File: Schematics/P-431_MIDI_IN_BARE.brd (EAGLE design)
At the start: 47.6 x 85.4 mm, 19 parts, among them X1 MIDI IN, X4 CTRL OUT and POWER

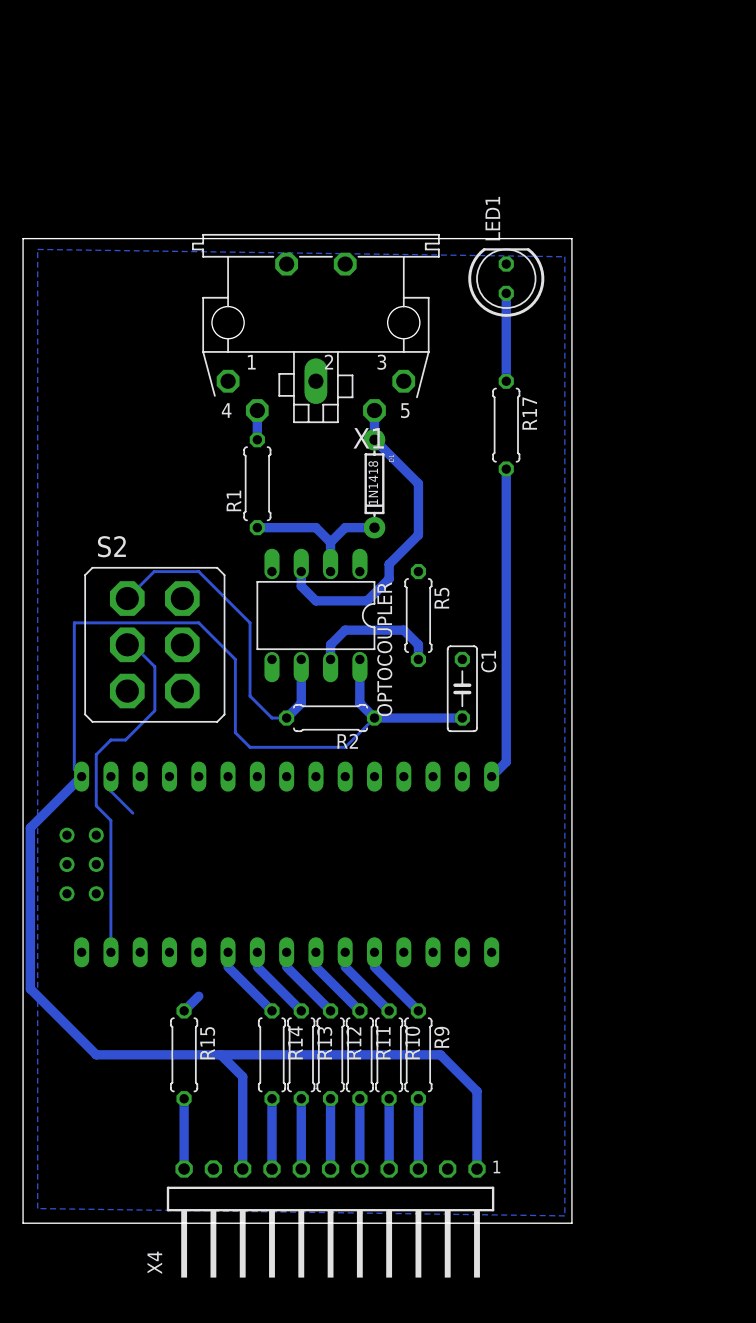
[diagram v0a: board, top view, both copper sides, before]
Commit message: Added reset pullup resistor and fixed resistors value for optocoupler
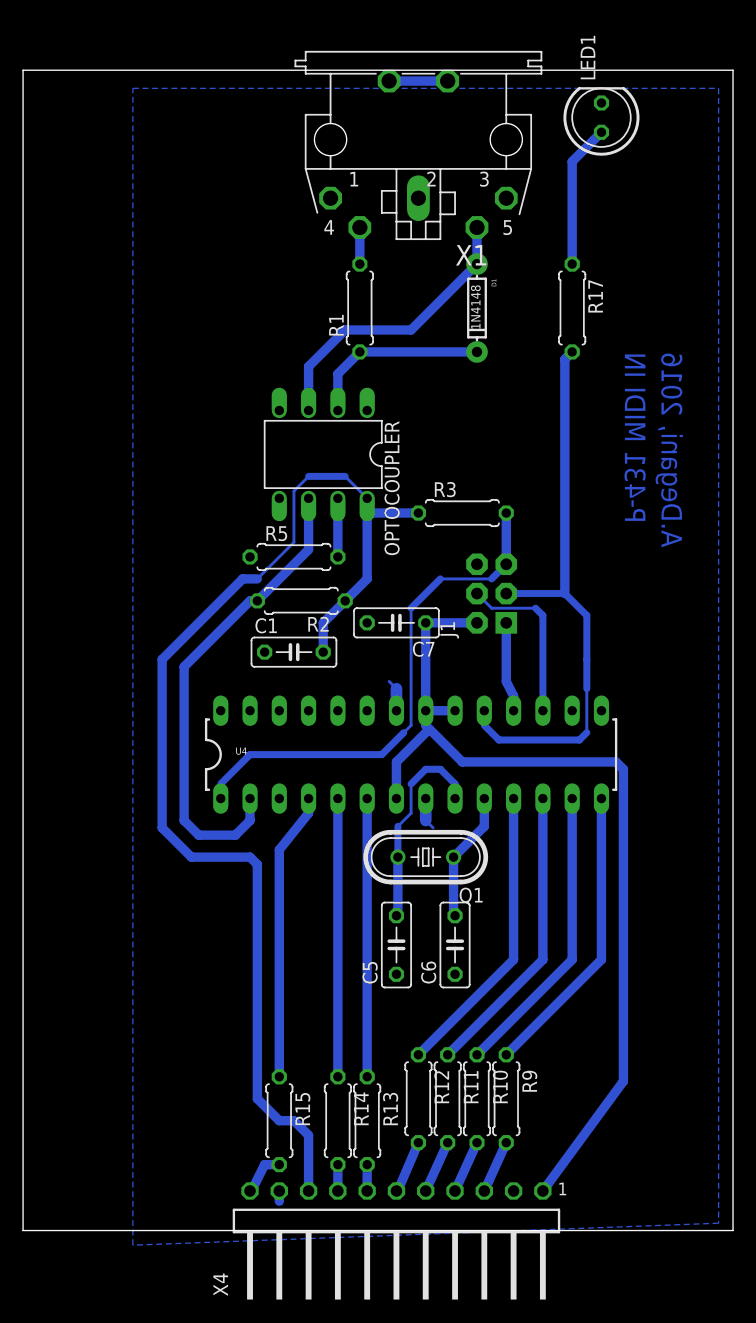
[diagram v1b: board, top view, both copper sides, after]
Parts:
- removed S2: PROG. SWITCH, switch:320-938
- removed U$1: NANO, Arduino-clone:NANO
- added C5, C6: 22pF, rcl:C050-025X075
- added C7: 100nF, rcl:C050-025X075
- added J1: AVR_SPI_PRG_6NS, SparkFun:2X3-NS
- added Q1: (no value), crystal:HC49/S
- added R3: 10K, resistor:0207/7
- added U4: ATMEGA328P_PDIP, SparkFun-DigitalIC:DIL28-3
- D1: value 1N1418 -> 1N4148
- moved X1 18.2 mm to (34.3, 94.0)
- moved R1 17.6 mm to (29.2, 79.4)
- moved D1 17.6 mm to (39.4, 79.4)
- moved LED1 16.2 mm to (50.2, 95.9)
- moved C1 14.9 mm to (23.5, 49.5), turned to 0 degrees
- moved OPTOCOUPLER 14.0 mm to (26.0, 66.7)
- moved R5 11.9 mm to (23.5, 57.8), turned to 0 degrees
- moved R17 11.7 mm to (47.6, 79.4)
- moved R2 10.5 mm to (24.1, 54.0)
- moved R15 10.0 mm to (22.2, 8.89)
- moved R10 8.52 mm to (39.4, 10.8)
- moved R11 8.52 mm to (36.8, 10.8)
- moved R12 8.52 mm to (34.3, 10.8)
- moved R9 8.52 mm to (41.9, 10.8)
- moved R13 8.08 mm to (29.8, 8.89)
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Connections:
- removed net !DS2_GATE: R15.1, U$1.D2
- removed net DS2_1: R9.1, U$1.D8
- removed net DS2_16: R13.1, U$1.D4
- removed net DS2_2: R10.1, U$1.D7
- removed net DS2_32: R14.1, U$1.D3
- removed net DS2_4: R11.1, U$1.D6
- removed net DS2_8: R12.1, U$1.D5
- removed net MIDI_IN_SW: S2.2, U$1.RX1
- new net !CNT_UP: U4.15
- new net !GATE: R15.1, U4.4
- new net A_RESET: J1.5, R3.2, U4.1
- new net B_1: R9.1, U4.14
- new net B_16: R13.1, U4.6
- new net B_2: R10.1, U4.13
- new net B_32: R14.1, U4.5
- new net B_4: R11.1, U4.12
- new net B_8: R12.1, U4.11
- new net CNT_CLR: U4.16
- new net N$26: C5.2, Q1.2, U4.9
- new net N$27: C6.2, Q1.1, U4.10
- new net POT_DI: J1.1, U4.18
- new net POT_SCK: J1.4, U4.17
- net +5V: now also C7.1, J1.2, R3.1, U4.20, U4.21, U4.7; no longer U$1.RAW
- net GND: now also C5.1, C6.1, C7.2, J1.6, U4.22, U4.8; no longer U$1.GND, U$1.GND1
- net MIDI_IN: now also U4.2; no longer S2.1
- net MIDI_LED: now also J1.3, U4.19; no longer U$1.D13
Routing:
- net A_RESET: track 0.00 -> 44.3 mm
- net +5V: track 142.2 -> 182.4 mm
- net MIDI_IN_SW: track 31.3 -> 0.00 mm
- net B_8: track 0.00 -> 25.6 mm
- net B_4: track 0.00 -> 25.6 mm
- net B_2: track 0.00 -> 25.6 mm
- net B_1: track 0.00 -> 25.6 mm
- net !GATE: track 0.00 -> 25.0 mm
- net B_32: track 0.00 -> 24.1 mm
- net B_16: track 0.00 -> 24.1 mm
- net MIDI_LED: track 27.2 -> 50.1 mm
- net N$26: track 0.00 -> 18.1 mm
- net POT_SCK: track 0.00 -> 14.8 mm
- net MIDI_IN: track 29.4 -> 41.5 mm
- net N$27: track 0.00 -> 11.3 mm
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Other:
- board size 47.6 x 85.4 mm -> 61.6 x 100.6 mm
- board text added: "A.Degani, 2016"
- board text added: "P-431 MIDI IN"
